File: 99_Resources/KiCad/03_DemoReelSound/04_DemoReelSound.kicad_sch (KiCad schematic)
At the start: 11 parts, among them J1 Conn_01x03_Pin, J4 Conn_01x03_Socket, U1 BlueToothAudioR

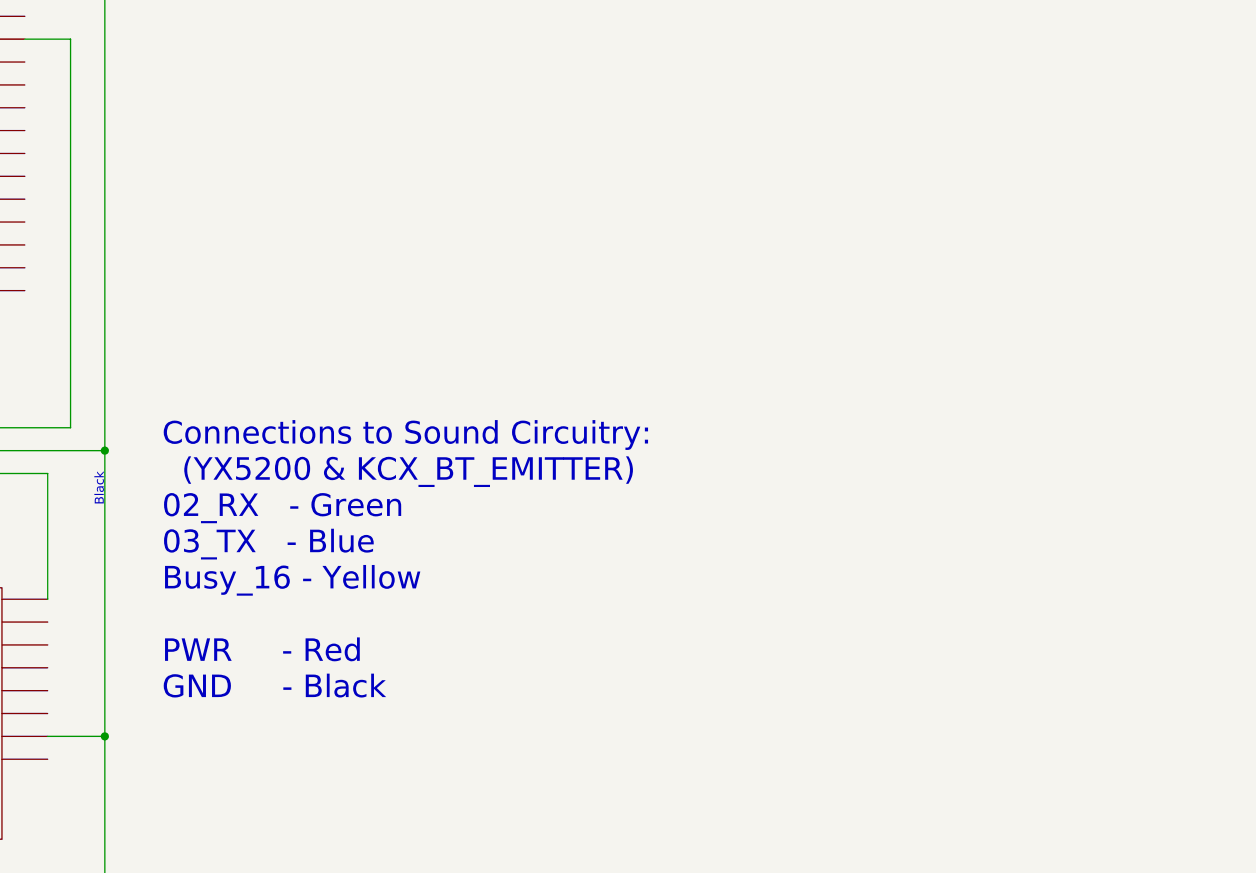
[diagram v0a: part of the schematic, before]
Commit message: begin moving 03_DemoReelSound to 04_DemoReelSound
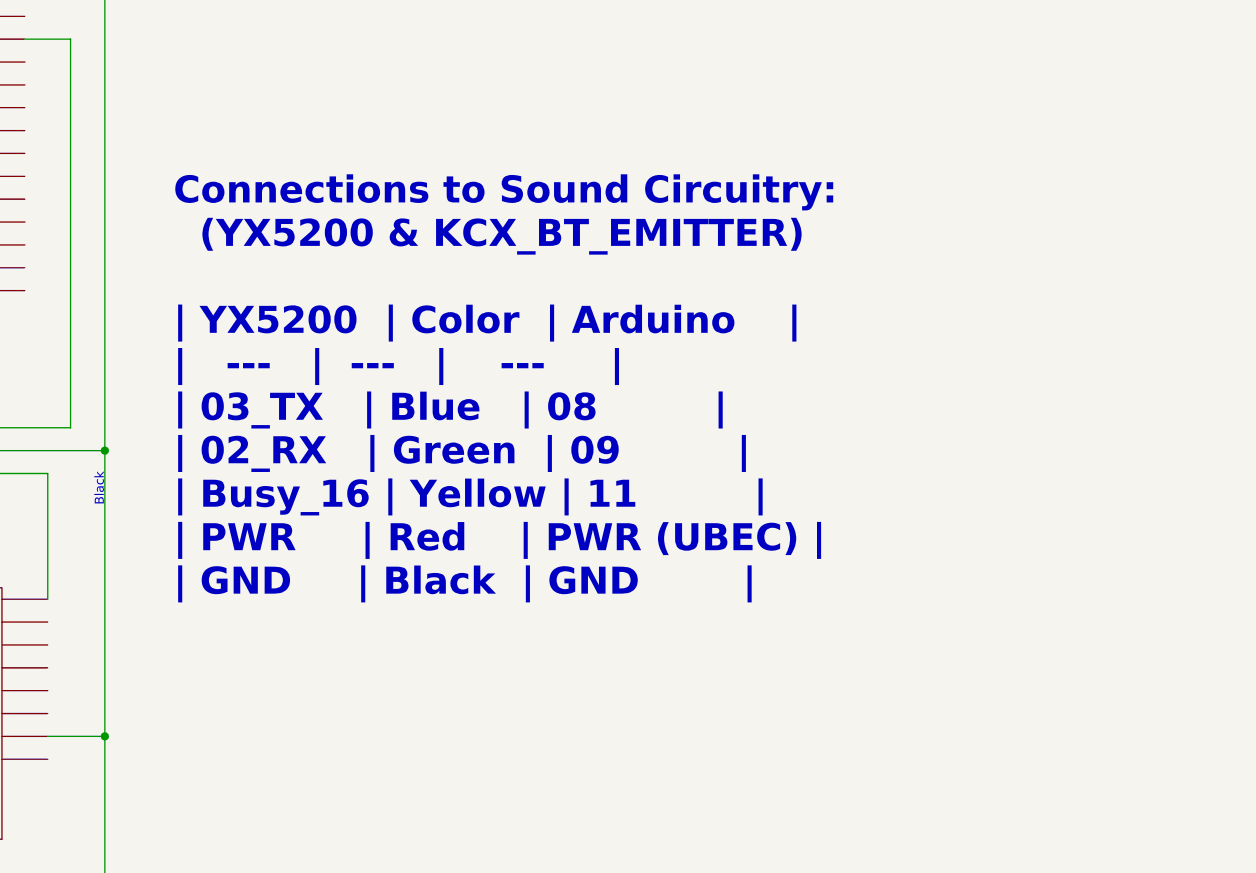
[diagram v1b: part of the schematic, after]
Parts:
- A?: symbol 03_DemoReelSound-rescue:Arduino_USB-mdoLibrary -> 04_DemoReelSound-rescue:Arduino_USB-mdoLibrary
- M?: symbol 03_DemoReelSound-rescue:HC-SR04-mdoLibrary -> 04_DemoReelSound-rescue:HC-SR04-mdoLibrary
- Z?: symbol 03_DemoReelSound-rescue:LEDring_big-mdoLibrary -> 04_DemoReelSound-rescue:LEDring_big-mdoLibrary
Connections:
- net at A?.~ (VIN): now also A1.~ (USB-_15)
- net at A1.~ (USB-_15): no longer A?.~ (VIN)
- net at Z?.~ (GND): now also A1.~ (USB-_15), U1.~ (TX)
- net at U1.~ (TX): now also J4.2 (Pin_2)
- new net: A?.~ (VIN), M?.~ (VCC), SW?.2
- new net: A?.~ (VIN), M?.~ (VCC) (x2)
- new net: A1.~ (USB-_15), A?.~ (VIN), J4.3 (Pin_3), U1.~ (TX), Z?.~ (GND)
- new net: A1.~ (USB-_15), A?.~ (VIN)
- new net: A1.~ (USB-_15), U1.~ (TX) (x3)
- now unconnected: A1.~ (USB-_15), A1.~ (USB-_15), A1.~ (USB-_15), A1.~ (USB-_15), A1.~ (USB-_15), A1.~ (USB-_15)
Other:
- note added: "Connections to Sound Circuitry: (YX5200 & KCX_BT_EMITTER) | YX5200 | Color | Arduino | | --- | --- | --- | | 03_TX | Blue | 08 | | 02_RX | Green | 09 | | Busy_16 | Yellow | 11 | | PWR | Red | PWR (UBEC) | | GND | Black | GND |"
- note removed: "Connections to Sound Circuitry: (YX5200 & KCX_BT_EMITTER) 02_RX - Green 03_TX - Blue Busy_16 - Yellow PWR - Red GND - Black"
- title: 03 Sonar Range Detector - DemoReelSound -> 04 Sonar Range Detector - DemoReelSound
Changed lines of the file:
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@@
   (paper "USLetter")
   (title_block
-    (title "03 Sonar Range Detector - DemoReelSound")
-    (date "2023-05-21")
+    (title "04 Sonar Range Detector - DemoReelSound")
+    (date "2023-06-10")
     (company "Author: https://github.com/Mark-MDO47/ArduinoClass/tree/master")
     (comment 1 "NOTE: Chips & Modules shown top view, notch at top")
@@
     (effects (font (size 1 1)) (justify right bottom))
   )
-  (text "Connections to Sound Circuitry:\n  (YX5200 & KCX_BT_EMITTER)\n02_RX   - Green\n03_TX   - Blue\nBusy_16 - Yellow\n\nPWR     - Red\nGND     - Black"
-    (at 161.29 170.18 0)
-    (effects (font (size 2.5 2.5)) (justify left bottom))
+  (text "Connections to Sound Circuitry:\n  (YX5200 & KCX_BT_EMITTER)\n\n| YX5200  | Color  | Arduino    |\n|   ---   |  ---   |    ---     |\n| 03_TX   | Blue   | 08         |\n| 02_RX   | Green  | 09         |\n| Busy_16 | Yellow | 11         |\n| PWR     | Red    | PWR (UBEC) |\n| GND     | Black  | GND        |"
+    (at 162.56 158.75 0)
+    (effects (font (face "Courier New") (size 3 3) (thickness 0.6) bold) (justify left bottom))
   )
   (text "Connection to ProgrammingArduino:\n1 - 9_TX - Yellow\n2 - 2_RX - Green\n3 - GND  - Black\n\nNote: label TX/RX refers to the KCX_BT_EMITTER chip.\nUsage in Programming Arduino is reversed from that."
@@
     (pin "2")
     (instances
-      (project "03_DemoReelSound"
+      (project "04_DemoReelSound"
         (path "/1f0f243b-db9e-4aa9-b961-93fb203fa709"
           (reference "R?") (unit 1)
@@
     (pin "2")
     (instances
-      (project "03_DemoReelSound"
+      (project "04_DemoReelSound"
         (path "/1f0f243b-db9e-4aa9-b961-93fb203fa709"
           (reference "SW?") (unit 1)
@@
     )
   )
-  (symbol (lib_id "03_DemoReelSound-rescue:Arduino_USB-mdoLibrary") (at 130.81 106.68 0) (unit 1)
+  (symbol (lib_id "04_DemoReelSound-rescue:Arduino_USB-mdoLibrary") (at 130.81 106.68 0) (unit 1)
     (in_bom yes) (on_board yes) (dnp no)
     (property "Reference" "A?" (at 130.81 81.28 0)
@@
     (pin "~")
     (instances
-      (project "03_DemoReelSound"
+      (project "04_DemoReelSound"
         (path "/1f0f243b-db9e-4aa9-b961-93fb203fa709"
           (reference "A?") (unit 1)
@@
     )
   )
-  (symbol (lib_id "03_DemoReelSound-rescue:HC-SR04-mdoLibrary") (at 73.66 116.84 0) (unit 1)
+  (symbol (lib_id "04_DemoReelSound-rescue:HC-SR04-mdoLibrary") (at 73.66 116.84 0) (unit 1)
     (in_bom yes) (on_board yes) (dnp no)
     (property "Reference" "M?" (at 77.6732 113.919 0)
@@
     (pin "~")
     (instances
-      (project "03_DemoReelSound"
+      (project "04_DemoReelSound"
         (path "/1f0f243b-db9e-4aa9-b961-93fb203fa709"
           (reference "M?") (unit 1)
@@
     )
   )
-  (symbol (lib_id "03_DemoReelSound-rescue:UBEC-mdoLibrary") (at 38.1 80.01 0) (unit 1)
+  (symbol (lib_id "04_DemoReelSound-rescue:UBEC-mdoLibrary") (at 38.1 80.01 0) (unit 1)
     (in_bom yes) (on_board yes) (dnp no)
     (property "Reference" "J?" (at 40.64 62.5602 0)
@@
     (pin "~")
     (instances
-      (project "03_DemoReelSound"
+      (project "04_DemoReelSound"
         (path "/1f0f243b-db9e-4aa9-b961-93fb203fa709"
           (reference "J?") (unit 1)
@@
     (pin "2")
     (instances
-      (project "03_DemoReelSound"
+      (project "04_DemoReelSound"
         (path "/1f0f243b-db9e-4aa9-b961-93fb203fa709"
           (reference "BT?") (unit 1)
@@
     )
   )
-  (symbol (lib_id "03_DemoReelSound-rescue:LEDring_big-mdoLibrary") (at 91.44 43.18 0) (unit 1)
+  (symbol (lib_id "04_DemoReelSound-rescue:LEDring_big-mdoLibrary") (at 91.44 43.18 0) (unit 1)
     (in_bom yes) (on_board yes) (dnp no)
     (property "Reference" "Z?" (at 117.5512 43.307 0)
@@
     (pin "~")
     (instances
-      (project "03_DemoReelSound"
+      (project "04_DemoReelSound"
         (path "/1f0f243b-db9e-4aa9-b961-93fb203fa709"
           (reference "Z?") (unit 1)
@@
     (pin "~")
     (instances
-      (project "03_DemoReelSound"
+      (project "04_DemoReelSound"
         (path "/1f0f243b-db9e-4aa9-b961-93fb203fa709"
           (reference "U1") (unit 1)
@@
     (pin "2")
     (instances
-      (project "03_DemoReelSound"
+      (project "04_DemoReelSound"
         (path "/1f0f243b-db9e-4aa9-b961-93fb203fa709"
           (reference "R1") (unit 1)
@@
     (pin "~")
     (instances
-      (project "03_DemoReelSound"
+      (project "04_DemoReelSound"
         (path "/1f0f243b-db9e-4aa9-b961-93fb203fa709"
           (reference "A1") (unit 1)
@@
     (pin "3")
     (instances
-      (project "03_DemoReelSound"
+      (project "04_DemoReelSound"
         (path "/1f0f243b-db9e-4aa9-b961-93fb203fa709"
           (reference "J4") (unit 1)
@@
     (pin "3")
     (instances
-      (project "03_DemoReelSound"
+      (project "04_DemoReelSound"
         (path "/1f0f243b-db9e-4aa9-b961-93fb203fa709"
           (reference "J1") (unit 1)
@@
     )
     (instances
-      (project "03_DemoReelSound"
+      (project "04_DemoReelSound"
         (path "/1f0f243b-db9e-4aa9-b961-93fb203fa709" (page "2"))
       )
